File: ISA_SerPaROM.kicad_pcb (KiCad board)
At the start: 2 copper layers, 176.5 x 102.9 mm, 91 parts, among them J1 ISA BUS, J10 Parallel Port, J11 Serial 4 IDC, J12 Serial 3 IDC, J13 UART4_SEL, J14 ROM Config, J2 ADDR_IRQ, J3 UART1_SEL, J4 UART2_SEL, J5 ADDR, J6 Serial 2 IDC, J7 Serial 1 DB9, J8 UART3_SEL, J9 Parport IRQ Select, U1 74LS138, U11 74LS30, U12 74LS86, U13 74LS02, U14 74LS155, U15 74LS245, U16 74LS174, U17 74LS374, U18 74LS05, U19 74LS125, U2 74LS138, U20 74LS240, U21 74LS244, U23 16C554, U24 74LS32, U25 GD75232N, U26 GD75232N, U27 SST39SF040, U28 74HCT688, U5 GD75232N, U6 GD75232N, X1 1.8432Mhz

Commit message: Add notes to the schematic, cleaned the silkscreen
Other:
- board text added: "32K"
- board text added: "64K"
- board text added: "A15"
- board text added: "A16"
- board text added: "A17"
- board text added: "A18"
- board text added: "ENA"
- board text added: "ROM EXP"

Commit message: Update mask and gerbers
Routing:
- net /A1: track 189.5 -> 190.6 mm

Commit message: Update silkscreen
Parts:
- U1, U2: value 74LS138 -> 74HCT138
- U24: value 74LS32 -> 74HCT32
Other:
- board text added: "10k bussed"
- board text added: "74HCT138"
- board text added: "74HCT32"
- board text added: "Serial / Parallel / ROM ISA Board - 1.1 by hkz"
- board text removed: "4.7k bussed"
- board text removed: "74LS138"
- board text removed: "74LS32"
- board text removed: "Serial / Parallel / ROM ISA Board - 1.0 by hkz"

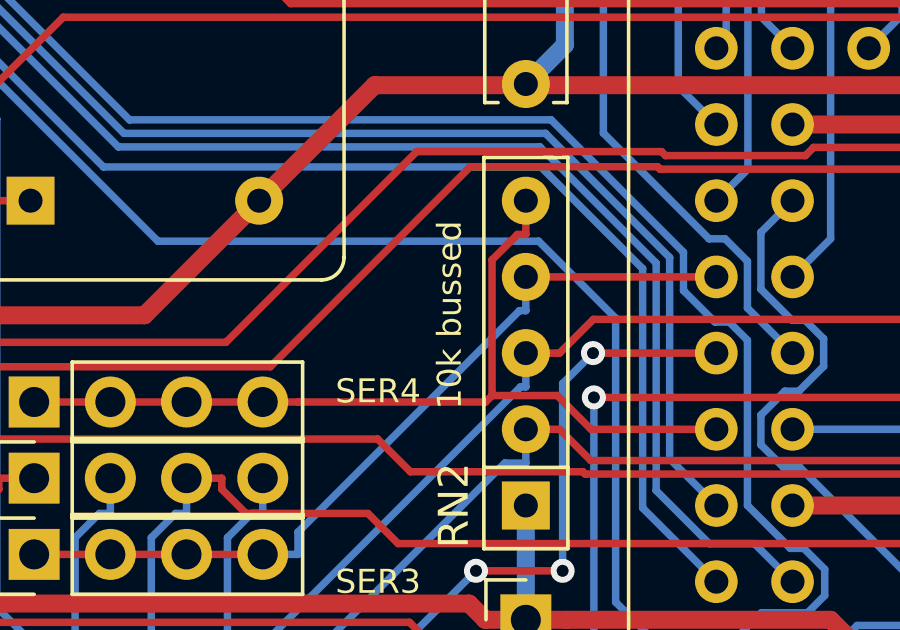
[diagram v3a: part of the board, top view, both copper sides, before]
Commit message: set resistor type for '554 pullup to 4.7k
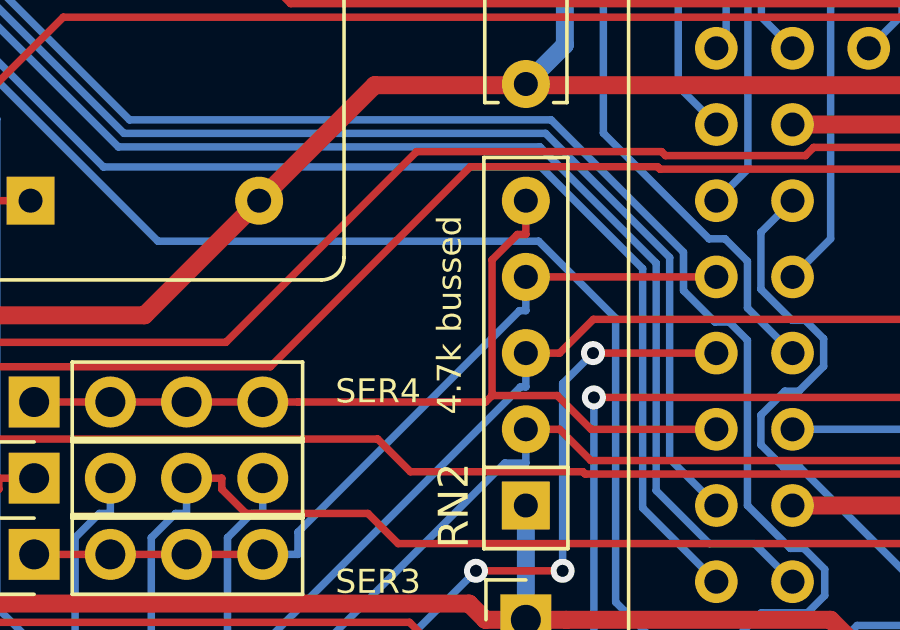
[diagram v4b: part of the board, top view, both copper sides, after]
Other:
- board text added: "4.7k bussed"
- board text removed: "10k bussed"

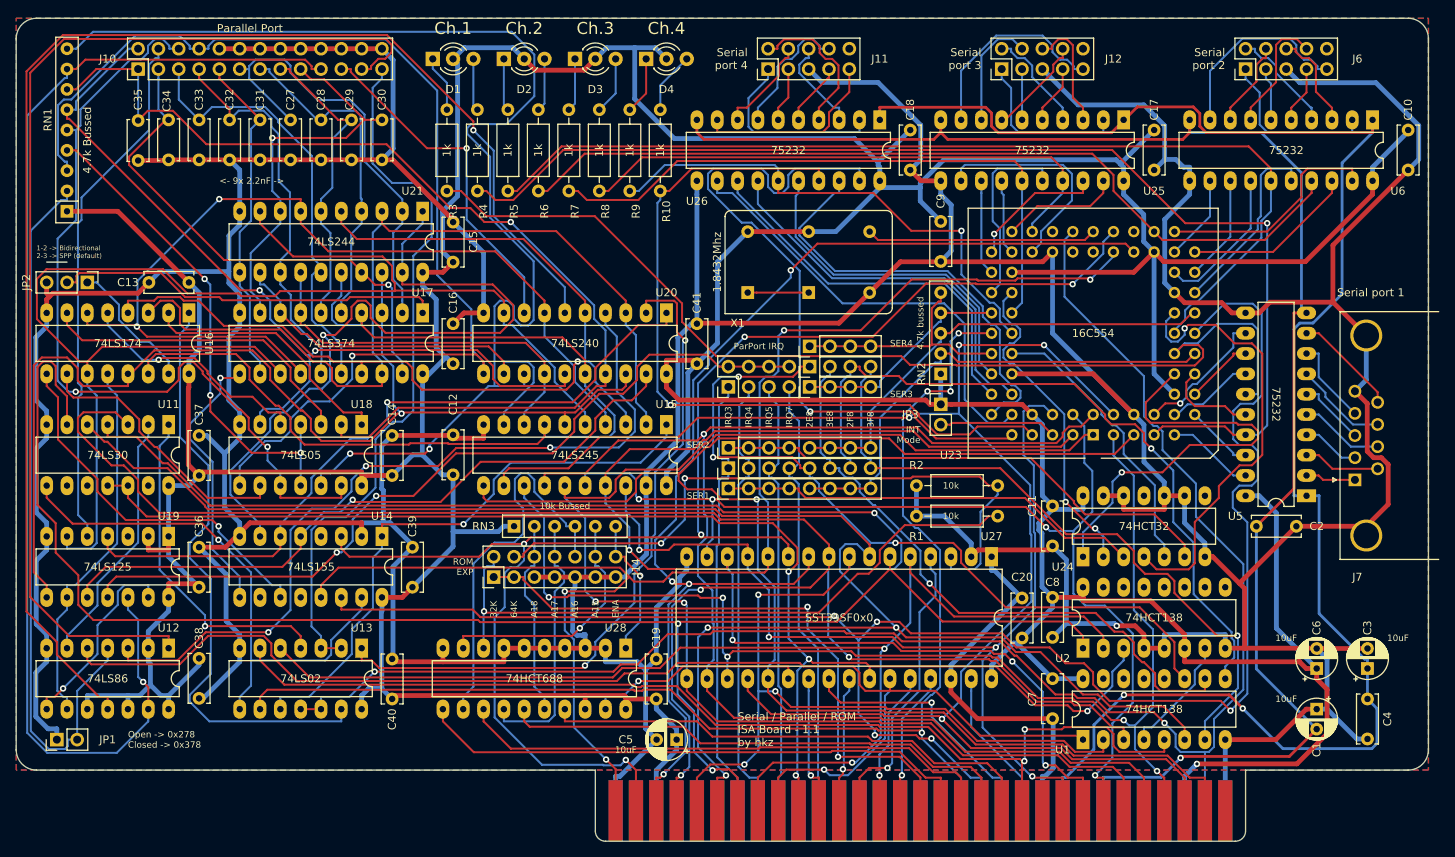
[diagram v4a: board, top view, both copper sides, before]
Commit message: Added LED bar and moved serial leds
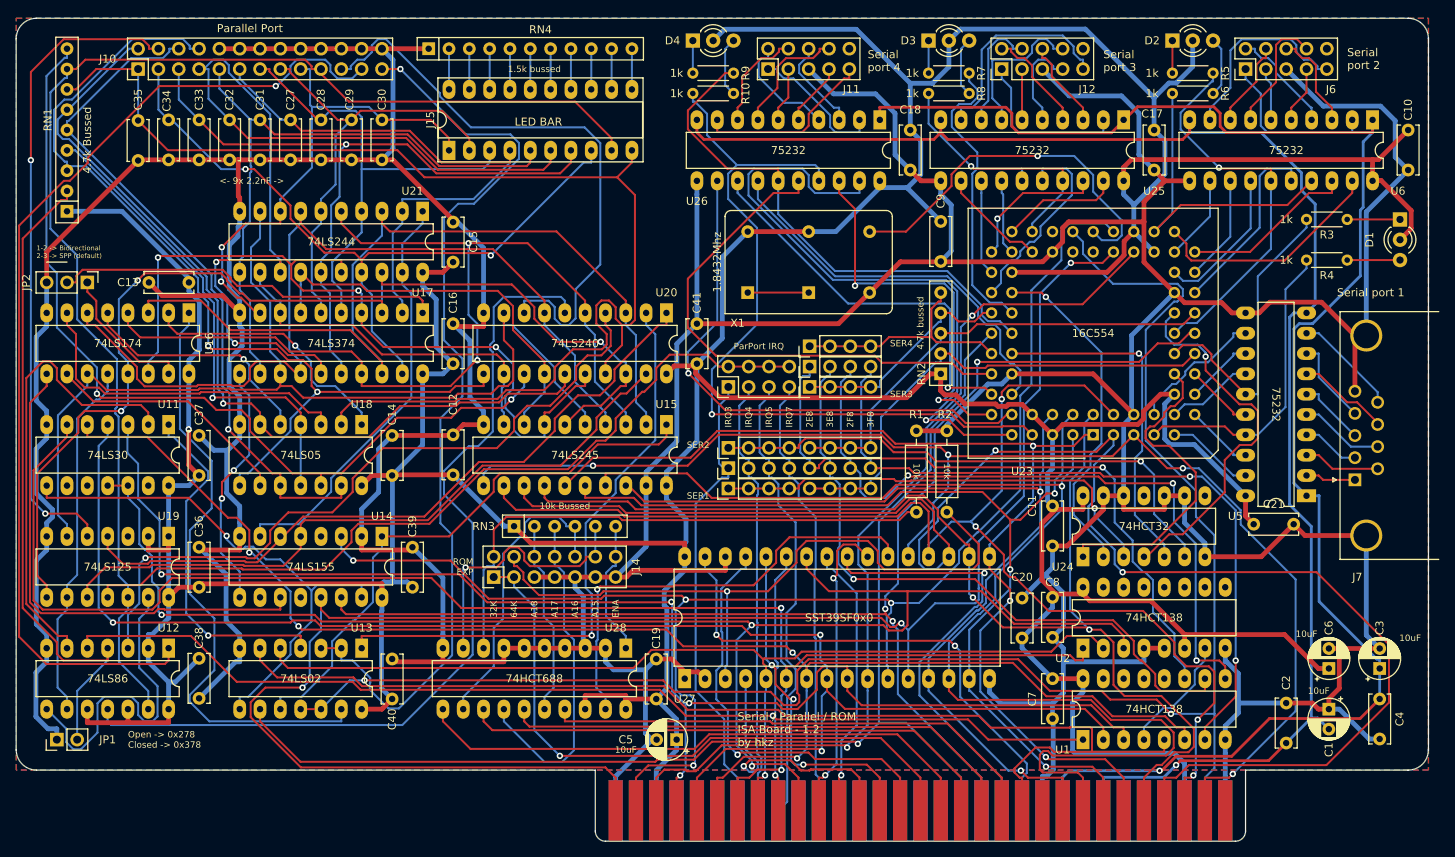
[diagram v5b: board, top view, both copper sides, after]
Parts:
- removed JP3: Interrupt Mode, Connector_PinHeader_2.54mm:PinHeader_1x02_P2.54mm_Vertical
- added C21: 100nF, Capacitor_THT:C_Disc_D6.0mm_W2.5mm_P5.00mm, F.Cu at (293.1, 163.6)
- added J15: LED Bar, Package_DIP:DIP-20_W7.62mm_Socket_LongPads, F.Cu at (192.5, 116.8)
- added RN4: 1.5k, Resistor_THT:R_Array_SIP11, F.Cu at (190.0, 104.1)
- R10, R3, R4, R5, R6, R7, R8, R9: footprint Resistor_THT:R_Axial_DIN0207_L6.3mm_D2.5mm_P10.16mm_Horizontal -> Resistor_THT:R_Axial_DIN0204_L3.6mm_D1.6mm_P5.08mm_Horizontal
- moved D1 122.6 mm to (311.4, 125.5), turned to 270 degrees
- moved R3 113.4 mm to (304.8, 125.5), turned to 180 degrees
- moved R4 110.3 mm to (304.8, 130.6), turned to 180 degrees
- moved R6 84.4 mm to (288.0, 109.7), turned to 180 degrees
- moved D2 83.6 mm to (283.0, 103.1)
- moved R5 83.2 mm to (283.0, 107.2), turned to 0 degrees
- moved R8 46.3 mm to (257.6, 109.7), turned to 180 degrees
- moved R7 45.2 mm to (252.5, 107.2), turned to 0 degrees
- moved D3 44.3 mm to (252.5, 103.1)
- moved U27 41.3 mm to (222.0, 182.9), turned to 90 degrees
- moved C2 22.1 mm to (297.2, 185.9), turned to 270 degrees
- moved R1 10.7 mm to (251.0, 151.9), turned to 270 degrees
- moved R10 9.37 mm to (228.1, 109.7), turned to 180 degrees
- moved R9 9.11 mm to (223.0, 107.2), turned to 0 degrees
- moved R2 7.83 mm to (254.8, 151.9), turned to 270 degrees
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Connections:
- U23 pad 31: (no net) -> VCC
- U23 pad 65: Net-(JP3-Pad2) -> VCC
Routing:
- net /RX_A: track 146.3 -> 38.2 mm, vias 1 -> 0
- net /TX_A: track 132.4 -> 38.2 mm
- net /TX_B: track 124.7 -> 48.6 mm, vias 0 -> 1
- net /PARPORT_DATA2: track 49.7 -> 119.8 mm, vias 0 -> 2
- net /RX_B: track 108.2 -> 40.5 mm
- net /PARPORT_IRQ: track 175.4 -> 110.6 mm, vias 1 -> 0
- net /~IOW: track 221.8 -> 164.3 mm, vias 5 -> 3
- net /D5: track 154.1 -> 200.3 mm, vias 5 -> 2
- net /~MEMW: track 19.1 -> 65.3 mm, vias 0 -> 2
- net /PARPORT_BD3: track 173.5 -> 129.8 mm
- net /A0: track 176.4 -> 219.8 mm, vias 4 -> 3
- net /D3: track 174.9 -> 132.3 mm, vias 2 -> 3
- net /RN_8: track 154.0 -> 113.0 mm
- net /D6: track 204.3 -> 163.7 mm
- net /PARPORT_DATA3: track 42.3 -> 80.5 mm
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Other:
- board text added: "1.5k bussed"
- board text added: "LED BAR"
- board text added: "Serial / Parallel / ROM ISA Board - 1.2 by hkz"
- board text removed: "Ch.1"
- board text removed: "Ch.2"
- board text removed: "Ch.3"
- board text removed: "Ch.4"
- board text removed: "INT Mode"
- board text removed: "Serial / Parallel / ROM ISA Board - 1.1 by hkz"

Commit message: Remove ROM, add buffer for uart
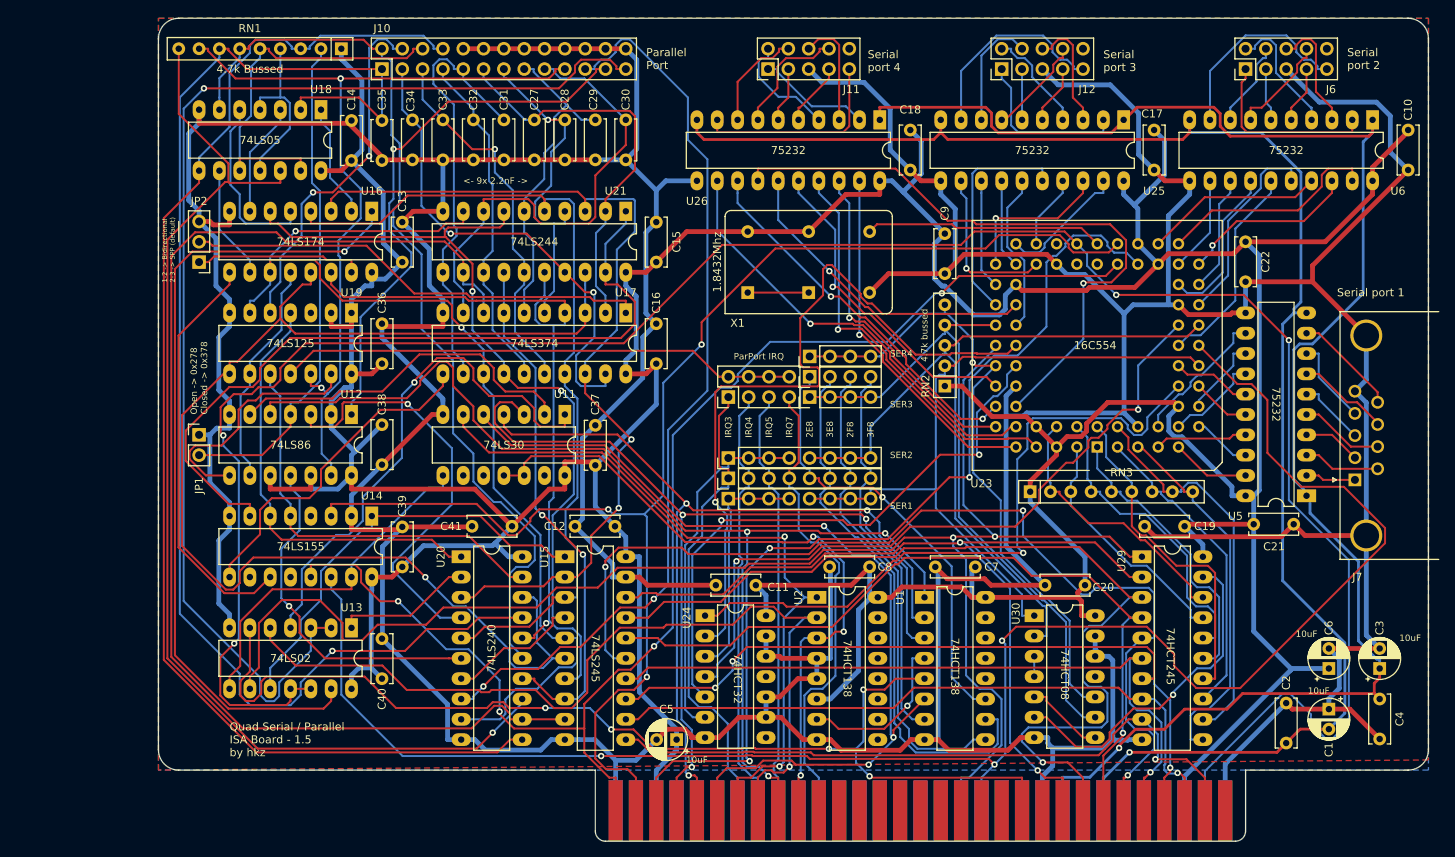
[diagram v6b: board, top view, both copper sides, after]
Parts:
- removed D1: LED Channel A, LED_THT:LED_D3.0mm-3
- removed D2: LED Channel B, LED_THT:LED_D3.0mm-3
- removed D3: LED Channel C, LED_THT:LED_D3.0mm-3
- removed D4: LED Channel D, LED_THT:LED_D3.0mm-3
- removed J14: ROM Config, Connector_PinHeader_2.54mm:PinHeader_2x07_P2.54mm_Vertical
- removed J15: LED Bar, Package_DIP:DIP-20_W7.62mm_Socket_LongPads
- removed R1, R2: 10k, Resistor_THT:R_Axial_DIN0207_L6.3mm_D2.5mm_P10.16mm_Horizontal
- removed R10, R3, R4, R5, R6, R7, R8, R9: 1k, Resistor_THT:R_Axial_DIN0204_L3.6mm_D1.6mm_P5.08mm_Horizontal
- removed RN4: 1.5k, Resistor_THT:R_Array_SIP11
- removed U27: SST39SF040, Package_DIP:DIP-32_W15.24mm_LongPads
- removed U28: 74HCT688, Package_DIP:DIP-20_W7.62mm_LongPads
- added C22: 100nF, Capacitor_THT:C_Disc_D6.0mm_W2.5mm_P5.00mm, F.Cu at (292.1, 128.3)
- added U29: 74HCT245, Package_DIP:DIP-20_W7.62mm_LongPads, F.Cu at (279.1, 167.6)
- added U30: 74HCT08, Package_DIP:DIP-14_W7.62mm_LongPads, F.Cu at (265.7, 175.0)
- RN2: value 4.7k -> 10k
- RN3: value 10k -> 10K; footprint Resistor_THT:R_Array_SIP6 -> Resistor_THT:R_Array_SIP9
- moved C19 69.5 mm to (284.5, 163.8), turned to 180 degrees
- moved RN3 64.7 mm to (265.2, 159.5)
- moved C37 49.5 mm to (210.8, 156.2)
- moved U11 49.5 mm to (207.0, 149.9)
- moved U24 47.8 mm to (224.5, 175.0), turned to 0 degrees
- moved JP1 42.0 mm to (161.3, 152.4), turned to 0 degrees
- moved RN1 39.9 mm to (179.1, 104.1), turned to 180 degrees
- moved U20 39.8 mm to (194.1, 167.6), turned to 0 degrees
- moved C14 39.7 mm to (180.3, 118.1)
- moved U18 39.7 mm to (176.5, 111.8)
- moved C11 38.4 mm to (230.9, 171.2), turned to 180 degrees
- moved C38 37.1 mm to (184.2, 151.1)
- moved U12 37.1 mm to (180.3, 149.9)
- moved C36 36.1 mm to (184.2, 143.5)
- moved U19 36.1 mm to (180.3, 137.2)
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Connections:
- net /PARPORT_RPA renamed /~PARPORT_RPA
- net /PARPORT_RPB renamed /~PARPORT_RPB
- net /PARPORT_RPC renamed /~PARPORT_RPC
- net /PARPORT_WPA renamed /~PARPORT_WPA
- net /PARPORT_WPC renamed /~PARPORT_WPC
- J1 pad 11: /~MEMW -> (no net)
- J1 pad 12: /~MEMR -> (no net)
- J1 pad 43: /A19 -> (no net)
- J1 pad 44: /A18 -> (no net)
- J1 pad 45: /A17 -> (no net)
- J1 pad 46: /A16 -> (no net)
- J1 pad 47: /A15 -> (no net)
- J1 pad 48: /A14 -> (no net)
- J1 pad 49: /A13 -> (no net)
- J1 pad 50: /A12 -> (no net)
- J1 pad 51: /A11 -> (no net)
- J1 pad 52: /A10 -> (no net)
- RN3 pad 2: /SW_A18 -> /UART-D0
- RN3 pad 3: /SW_A17 -> /UART-D1
- RN3 pad 4: /SW_A16 -> /UART-D2
- RN3 pad 5: /SW_A15 -> /UART-D3
- RN3 pad 6: /SW_ROM_EN -> /UART-D4
- U23 pad 1: /D3 -> /UART-D3
- U23 pad 2: /D4 -> /UART-D4
- U23 pad 3: /D5 -> /UART-D5
- U23 pad 4: /D6 -> /UART-D6
- U23 pad 5: /D7 -> /UART-D7
- U23 pad 66: /D0 -> /UART-D0
- U23 pad 67: /D1 -> /UART-D1
- U23 pad 68: /D2 -> /UART-D2
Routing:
- net /A9: track 195.2 -> 86.2 mm
- net /PARPORT_BD7: track 45.9 -> 152.9 mm
- net /D5: track 200.3 -> 93.5 mm, vias 2 -> 3
- net /A6: track 193.5 -> 90.1 mm
- net VCC: track 778.1 -> 679.4 mm, vias 1 -> 0
- net /FLASH_A15: track 86.7 -> 0.00 mm, vias 1 -> 0
- net /A4: track 191.2 -> 109.0 mm
- net /D7: track 166.0 -> 85.0 mm, vias 4 -> 1
- net /A15: track 79.4 -> 0.00 mm, vias 1 -> 0
- net /D6: track 163.7 -> 84.9 mm, vias 4 -> 1
- net /PARPORT_DATA2: track 119.8 -> 43.2 mm, vias 2 -> 0
- net /A5: track 188.0 -> 115.1 mm, vias 4 -> 3
- net /A16: track 72.3 -> 0.00 mm
- net /COMPARATOR_A15: track 69.9 -> 0.00 mm
- net /RESETDRV: track 213.9 -> 283.1 mm, vias 2 -> 4
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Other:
- board size 176.5 x 102.9 mm -> 158.8 x 102.9 mm
- board text added: "74HCT08"
- board text added: "74HCT245"
- board text added: "Quad Serial / Parallel ISA Board - 1.5 by hkz"
- board text removed: "1.5k bussed"
- board text removed: "10k"
- board text removed: "10k Bussed"
- board text removed: "1k"
- board text removed: "32K"
- board text removed: "64K"
- board text removed: "74HCT688"
- board text removed: "A15"
- board text removed: "A16"
- board text removed: "A17"
- board text removed: "A18"
- board text removed: "ENA"
- board text removed: "LED BAR"
- board text removed: "ROM EXP"
- board text removed: "SST39SF0x0"
- board text removed: "Serial / Parallel / ROM ISA Board - 1.2 by hkz"

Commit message: Add new gerber, use 74HCT21
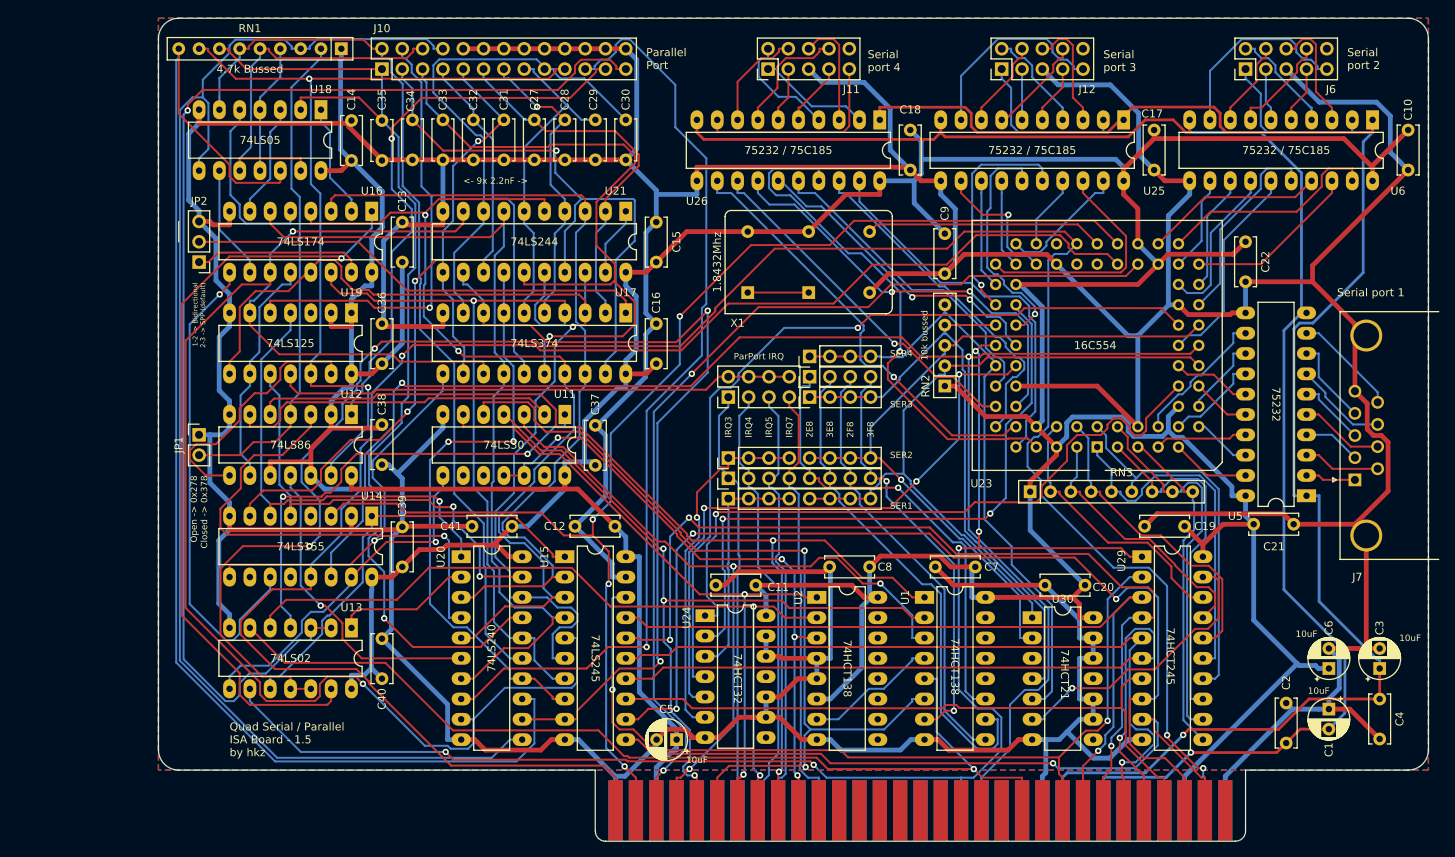
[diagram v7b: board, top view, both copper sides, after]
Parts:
- U30: value 74HCT08 -> 74HCT21
- moved U30 0.36 mm to (265.4, 175.3)
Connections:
- U30 pad 10: /~UART4_CS -> GND
- U30 pad 3: Net-(U30-Pad3) -> (no net)
- U30 pad 4: Net-(U30-Pad3) -> /~UART3_CS
- U30 pad 5: Net-(U30-Pad5) -> /~UART4_CS
- U30 pad 8: Net-(U30-Pad5) -> (no net)
- U30 pad 9: /~UART3_CS -> GND
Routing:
- net /PARPORT_BD3: track 134.7 -> 192.9 mm
- net /PARPORT_BD7: track 152.9 -> 106.0 mm, vias 0 -> 2
- net /D6: track 84.9 -> 126.5 mm, vias 1 -> 3
- net /PARPORT_DATA1: track 47.0 -> 87.8 mm
- net /RN_6: track 168.0 -> 129.6 mm
- net /RESETDRV: track 283.1 -> 247.4 mm
- net /A0: track 167.0 -> 202.6 mm, vias 4 -> 1
- net /D3: track 126.5 -> 92.7 mm, vias 3 -> 1
- net /PARPORT_BD4: track 158.5 -> 124.8 mm
- net /~CTS_D: track 79.7 -> 53.0 mm, vias 1 -> 2
- net /~IOW: track 221.9 -> 197.3 mm, vias 3 -> 2
- net /D1: track 119.2 -> 97.1 mm
- net /RN_8: track 142.1 -> 161.5 mm, vias 1 -> 0
- net /~PARPORT_RPA: track 95.6 -> 78.7 mm, vias 0 -> 2
- net /A3: track 115.5 -> 98.9 mm
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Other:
- board text added: "10k bussed"
- board text added: "74HCT21"
- board text added: "75232 / 75C185"
- board text removed: "4.7k bussed"
- board text removed: "74HCT08"
